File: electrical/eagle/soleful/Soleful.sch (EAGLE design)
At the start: 115 parts, among them IC1 STM32F405RGT, IC2 MCP1703DB, IC3 STM32F405RGT, Q1 MOSFET-PCHANNEL, Q2 8MHz, Q3 32.768kHz, Q4 32.768kHz, SW1 RST, SW2 USR, U1 MCP1802, Y1 12 MHz

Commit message: More work
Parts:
- added CN1: (no value), microbuilder:JST_2PIN
- added U3: MIC2090-1YM5TR, Micrel_By_element14_Batch_1:MIC2090-1YM5TR
- Q1: value MOSFET-PCHANNEL -> MOSFET
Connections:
- removed net N$10: Q1.D
- new net B: U3.EN
- new net VBAT: CN1.1, Q1.D
- new net VBUS: D1.ANODE, Q1.G, R10.2, R18.2, U$10.VUSB, U3.VOUT
- net 3V3: no longer D1.CATHODE, Q1.S
- net GND: now also CN1.2, U3.GND
- net N$8: now also U3.FAULT/; no longer D1.ANODE, Q1.G, R10.2, R18.2, U$10.VUSB
- net V+: now also D1.CATHODE, Q1.S, U3.VIN
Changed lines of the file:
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@@
 <part name="R18" library="SparkFun-Resistors" deviceset="100KOHM" device="-0603-1/10W-1%" value="100k"/>
 <part name="GND19" library="SparkFun-PowerSymbols" deviceset="GND" device=""/>
-<part name="Q1" library="User-Submitted" deviceset="MOSFET-PCHANNEL" device=""/>
-<part name="SUPPLY10" library="SparkFun-PowerSymbols" deviceset="VCC" device="" value="3V3"/>
+<part name="Q1" library="User-Submitted" deviceset="MOSFET-PCHANNEL" device="" value="MOSFET"/>
 <part name="GND20" library="supply1" deviceset="GND" device=""/>
 <part name="GND21" library="supply1" deviceset="GND" device=""/>
@@
 <part name="R37" library="rcl" deviceset="R-EU_" device="R0603" value="10k"/>
 <part name="R38" library="rcl" deviceset="R-EU_" device="R0805" value="0"/>
+<part name="U3" library="Micrel_By_element14_Batch_1" deviceset="MIC2090-1YM5TR" device=""/>
+<part name="GND42" library="Icotech_Eagle_Library" deviceset="GND" device=""/>
+<part name="SUPPLY11" library="SparkFun-PowerSymbols" deviceset="VCC" device="" value="V+"/>
+<part name="CN1" library="microbuilder" deviceset="JST_2PIN" device=""/>
+<part name="GND43" library="Icotech_Eagle_Library" deviceset="GND" device=""/>
+<part name="SUPPLY10" library="SparkFun-PowerSymbols" deviceset="VCC" device="" value="V+"/>
 </parts>
 <sheets>
@@
 <instance part="GND19" gate="1" x="238.76" y="233.68"/>
 <instance part="Q1" gate="G$1" x="228.6" y="259.08" rot="R90"/>
+<instance part="U3" gate="A" x="185.42" y="243.84"/>
+<instance part="GND42" gate="1" x="167.64" y="228.6"/>
+<instance part="SUPPLY11" gate="G$1" x="160.02" y="256.54"/>
+<instance part="CN1" gate="G$1" x="203.2" y="261.62"/>
+<instance part="GND43" gate="1" x="200.66" y="254"/>
 <instance part="SUPPLY10" gate="G$1" x="251.46" y="261.62"/>
 </instances>
@@
 <pinref part="C14" gate="G$1" pin="1"/>
 </segment>
-<segment>
-<pinref part="D1" gate="G$1" pin="CATHODE"/>
-<wire x1="243.84" y1="226.06" x2="251.46" y2="226.06" width="0.1524" layer="91"/>
-<wire x1="254" y1="226.06" x2="251.46" y2="226.06" width="0.1524" layer="91"/>
-<wire x1="251.46" y1="226.06" x2="251.46" y2="259.08" width="0.1524" layer="91"/>
-<pinref part="Q1" gate="G$1" pin="S"/>
-<wire x1="251.46" y1="259.08" x2="233.68" y2="259.08" width="0.1524" layer="91"/>
-<wire x1="251.46" y1="259.08" x2="251.46" y2="261.62" width="0.1524" layer="91"/>
-<junction x="251.46" y="259.08"/>
-<pinref part="SUPPLY10" gate="G$1" pin="VCC"/>
-</segment>
 </net>
 <net name="PB15-Y8" class="0">
@@
 <pinref part="GND19" gate="1" pin="GND"/>
 </segment>
+<segment>
+<pinref part="U3" gate="A" pin="GND"/>
+<wire x1="167.64" y1="236.22" x2="167.64" y2="231.14" width="0.1524" layer="91"/>
+<pinref part="GND42" gate="1" pin="GND"/>
+</segment>
+<segment>
+<pinref part="CN1" gate="G$1" pin="2"/>
+<wire x1="200.66" y1="261.62" x2="200.66" y2="256.54" width="0.1524" layer="91"/>
+<pinref part="GND43" gate="1" pin="GND"/>
+</segment>
 </net>
 <net name="N$1" class="0">
@@
 <pinref part="SUPPLY7" gate="G$1" pin="VCC"/>
 </segment>
+<segment>
+<pinref part="U3" gate="A" pin="VIN"/>
+<wire x1="167.64" y1="246.38" x2="160.02" y2="246.38" width="0.1524" layer="91"/>
+<wire x1="160.02" y1="246.38" x2="160.02" y2="256.54" width="0.1524" layer="91"/>
+<pinref part="SUPPLY11" gate="G$1" pin="VCC"/>
+</segment>
+<segment>
+<pinref part="D1" gate="G$1" pin="CATHODE"/>
+<wire x1="243.84" y1="226.06" x2="251.46" y2="226.06" width="0.1524" layer="91"/>
+<wire x1="251.46" y1="226.06" x2="251.46" y2="259.08" width="0.1524" layer="91"/>
+<pinref part="Q1" gate="G$1" pin="S"/>
+<wire x1="251.46" y1="259.08" x2="233.68" y2="259.08" width="0.1524" layer="91"/>
+<wire x1="251.46" y1="259.08" x2="251.46" y2="261.62" width="0.1524" layer="91"/>
+<junction x="251.46" y="259.08"/>
+<pinref part="SUPPLY10" gate="G$1" pin="VCC"/>
+</segment>
 </net>
 <net name="N$4" class="0">
@@
 </segment>
 </net>
-<net name="N$8" class="0">
+<net name="VBUS" class="0">
 <segment>
 <pinref part="U$10" gate="G$1" pin="VUSB"/>
@@
 <pinref part="Q1" gate="G$1" pin="G"/>
 <wire x1="228.6" y1="251.46" x2="233.68" y2="251.46" width="0.1524" layer="91"/>
-</segment>
-</net>
-<net name="N$10" class="0">
+<label x="226.06" y="226.06" size="1.778" layer="95"/>
+<wire x1="226.06" y1="226.06" x2="215.9" y2="226.06" width="0.1524" layer="91"/>
+<wire x1="215.9" y1="226.06" x2="215.9" y2="238.76" width="0.1524" layer="91"/>
+<junction x="226.06" y="226.06"/>
+<wire x1="215.9" y1="238.76" x2="203.2" y2="238.76" width="0.1524" layer="91"/>
+<pinref part="U3" gate="A" pin="VOUT"/>
+<wire x1="203.2" y1="243.84" x2="203.2" y2="238.76" width="0.1524" layer="91"/>
+</segment>
+</net>
+<net name="VBAT" class="0">
 <segment>
 <pinref part="Q1" gate="G$1" pin="D"/>
 <wire x1="223.52" y1="259.08" x2="210.82" y2="259.08" width="0.1524" layer="91"/>
-<wire x1="210.82" y1="259.08" x2="210.82" y2="261.62" width="0.1524" layer="91"/>
-</segment>
-</net>
+<pinref part="CN1" gate="G$1" pin="1"/>
+<wire x1="200.66" y1="264.16" x2="200.66" y2="269.24" width="0.1524" layer="91"/>
+<wire x1="200.66" y1="269.24" x2="210.82" y2="269.24" width="0.1524" layer="91"/>
+<wire x1="210.82" y1="269.24" x2="210.82" y2="259.08" width="0.1524" layer="91"/>
+<wire x1="210.82" y1="269.24" x2="210.82" y2="271.78" width="0.1524" layer="91"/>
+<junction x="210.82" y="269.24"/>
+<label x="208.28" y="271.78" size="1.778" layer="95"/>
+</segment>
+</net>
+<net name="N$8" class="0">
+<segment>
+<pinref part="U3" gate="A" pin="FAULT/"/>
+<wire x1="203.2" y1="246.38" x2="210.82" y2="246.38" width="0.1524" layer="91"/>
+</segment>
+</net>
+<net name="B" class="0">
+<segment>
+<pinref part="U3" gate="A" pin="EN"/>
+<wire x1="167.64" y1="241.3" x2="154.94" y2="241.3" width="0.1524" layer="91"/>
+<label x="162.56" y="241.3" size="1.778" layer="95"/>
+</segment>
+</net>

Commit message: Finally worked
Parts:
- removed C11B, C12B: 2u2, rcl:C-EUC0603
- removed C21, C22, C23, C24, C25, C26, C31, C32, C33: 100n, rcl:C-EUC0603
- removed C27, C28, C34, C35: 12p, rcl:C-EUC0603
- removed C29, C36, C37: 1u, rcl:C-EUC0603
- removed C30: 4u7, rcl:C-EUC0603
- removed D6: 1N5819, pyboard:1N5819
- removed IC3: STM32F405RGT, pyboard:STM32F405RGT
- removed JBL, JBR1, JBR2, JBR3, JBR4: 1, pinhead:PINHD-1X1
- removed JBOT: 8, pinhead:PINHD-1X8
- removed JLEFT: 14, pinhead:PINHD-1X14
- removed JPOW: 8, pinhead:PINHD-2X4
- removed JRIGHT: 11, pinhead:PINHD-1X11
- removed Q2: 8MHz, pyboard:TXC-CRYSTAL50X32
- removed Q3: 32.768kHz, pyboard:TXC-CRYSTAL32X15
- removed R19, R22: 22, rcl:R-EU_R0603
- removed R23, R37: 10k, rcl:R-EU_R0603
- removed R24, R25, R26, R27: 560, rcl:R-EU_R0603
- removed R28, R29: 4k7, rcl:R-EU_R0603
- removed R30, R31: 1k, rcl:R-EU_R0603
- removed R32, R34, R35: 100k, rcl:R-EU_R0603
- removed R33: 10M, rcl:R-EU_R0603
- removed R36: 0, rcl:R-EU_R0603
- removed R38: 0, rcl:R-EU_R0805
- removed U$2, U$3: KMR4TACTILE, pyboard:KMR4TACTILE
- removed U$4: MOLEX-SD-105027, pyboard:MOLEX-SD-105027
- removed U$5: MMA7660, pyboard:MMA7660
- removed U$6, U$7: LTST-C195KGJRKT, pyboard:LTST-C195KGJRKT
- removed U$8: USB-MICRO-AB, pyboard:USB-MICRO-AB
- removed U1: MCP1802, pyboard:MCP1802
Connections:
- removed net +3V3: C21.1, C22.1, C23.1, C24.1, C25.1, C26.1, C29.1, C30.1, C32.1, C37.1, IC3.VBAT, IC3.VDD@19, IC3.VDD@32, IC3.VDD@48, IC3.VDD@64, IC3.VDDA, JBL.1, JLEFT.1, R23.1, R28.1, R29.1, U$4.VDD, U$5.DVDD, U$6.A1, U$6.A2, U$7.A1, U$7.A2, U1.VOUT
- removed net BOOT0: IC3.BOOT0, JBOT.1, R35.1
- removed net FS_DM: IC3.PA11, R19.2
- removed net FS_DP: IC3.PA12, R22.2
- removed net FS_VUSB: IC3.PA9, R30.2
- removed net IO_PA0: IC3.PA0, JBR4.1
- removed net IO_PA1: IC3.PA1, JBR3.1
- removed net IO_PA14: IC3.PA14, JLEFT.9
- removed net IO_PA15: IC3.PA15, JLEFT.10
- removed net IO_PA2: IC3.PA2, JBR2.1
- removed net IO_PA3: IC3.PA3, JBR1.1
- removed net IO_PA4: IC3.PA4, JRIGHT.11
- removed net IO_PA5: IC3.PA5, JRIGHT.10
- removed net IO_PA6: IC3.PA6, JRIGHT.9
- removed net IO_PA7: IC3.PA7, JRIGHT.8
- removed net IO_PB0: IC3.PB0, JRIGHT.7
- removed net IO_PB1: IC3.PB1, JRIGHT.6
- removed net IO_PB10: IC3.PB10, JRIGHT.5
- removed net IO_PB11: IC3.PB11, JRIGHT.4, R32.1
- removed net IO_PB12: IC3.PB12, JRIGHT.3
- removed net IO_PB13: IC3.PB13, JLEFT.3
- removed net IO_PB14: IC3.PB14, JLEFT.4
- removed net IO_PB15: IC3.PB15, JLEFT.5
- removed net IO_PB2: IC3.PB2, R31.1
- removed net IO_PB3: IC3.PB3, JLEFT.11
- removed net IO_PB4: IC3.PB4, JLEFT.12
- removed net IO_PB9: IC3.PB9, JBOT.4
- removed net IO_PC0: IC3.PC0, JBOT.5
- removed net IO_PC1: IC3.PC1, JBOT.6
- removed net IO_PC2: IC3.PC2, JBOT.7
- removed net IO_PC3: IC3.PC3, JBOT.8
- removed net IO_PC6: IC3.PC6, JLEFT.6
- removed net IO_PC7: IC3.PC7, JLEFT.7
- removed net LEDG1: IC3.PC4, R24.1
- removed net LEDG2: IC3.PC5, R27.1
- removed net LEDR1: IC3.PA8, R26.1
- removed net LEDR2: IC3.PA10, R25.1, R36.2
- removed net MMA_AVDD: C33.1, IC3.PB5, R34.1, U$5.AVDD
- removed net MMA_INT: IC3.PB8, JBOT.3, U$5.INT
- removed net MMA_SCL: IC3.PB6, JLEFT.13, R29.2, U$5.SCL
- removed net MMA_SDA: IC3.PB7, JLEFT.14, R28.2, U$5.SDA
- removed net N$11: C12B.1, IC3.VCAP_1
- removed net N$12: R22.1, U$8.D+
- removed net N$13: C28.2, IC3.PH0, Q2.P$1
- removed net N$14: R24.2, U$6.K1
- removed net N$15: R25.2, U$7.K2
- removed net N$16: R26.2, U$6.K2
- removed net N$17: C35.2, IC3.PC14, Q3.P$1
- removed net N$18: C34.2, IC3.PC15, Q3.P$2
- removed net N$19: C27.2, IC3.PH1, Q2.P$2
- removed net N$20: R27.2, U$7.K1
- removed net N$21: R19.1, U$8.D-
- removed net N$22: R36.1, U$8.ID
- removed net N$23: R37.2, U$3.1@A, U$3.1@B
- removed net N$9: C11B.1, IC3.VCAP_2
- removed net NRST: C31.1, IC3.NRST, JBOT.2, R23.2, U$2.1@A, U$2.1@B
- removed net SDIO_CK: IC3.PC12, U$4.CLK
- removed net SDIO_CMD: IC3.PD2, U$4.CMD
- removed net SDIO_D0: IC3.PC8, U$4.DAT0
- removed net SDIO_D1: IC3.PC9, U$4.DAT1
- removed net SDIO_D2: IC3.PC10, U$4.DAT2
- removed net SDIO_D3: IC3.PC11, R33.1, U$4.DAT3
- removed net SDIO_SW: IC3.PC13, U$4.SWITCH
- removed net USR_SW: IC3.PA13, JLEFT.8, R37.1
- removed net VIN: C36.1, D6.K, JPOW.2, JPOW.4, JPOW.6, JPOW.8, JRIGHT.1, R38.1, U1.EN, U1.VIN
- removed net VUSB: D6.A, R30.1, R38.2, U$8.VUSB
- net GND: no longer C11B.2, C12B.2, C21.2, C22.2, C23.2, C24.2, C25.2, C26.2, C27.1, C28.1, C29.2, C30.2, C31.2, C32.2, C33.2, C34.1, C35.1, C36.2, C37.2, IC3.VSS@18, IC3.VSS@63, IC3.VSSA, JLEFT.2, JPOW.1, JPOW.3, JPOW.5, JPOW.7, JRIGHT.2, R31.2, R32.2, R33.2, R34.2, R35.2, U$2.0@A, U$2.0@B, U$3.0@A, U$3.0@B, U$4.VSS, U$5.AVSS, U$5.DVSS, U$5.N/C@10, U$5.N/C@2, U$5.RSRVD, U$8.GND, U1.GND
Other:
- note removed: "Analog"
- note removed: "DFU boot"
- note removed: "MMA"
- note removed: "R16 and R18 are unpopulated. Used for optional USB OTG support."
- note removed: "VBAT"
- note removed: "VDD"

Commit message: Added IMU files
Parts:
- added C21, C22: 22pF, microbuilder:CAP_CERAMIC0805-NOOUTLINE
- added C23: 0.1uF, microbuilder:CAP_CERAMIC0805-NOOUTLINE
- added C24: 0.1uF, microbuilder:CAP_CERAMIC0805_10MGAP
- added D6: 1n4148, microbuilder:DIODESOD-323
- added Q2, Q3: BSS138, microbuilder:MOSFET-NWIDE
- added R19, R22, R23, R24, R25, R28: 10K, microbuilder:RESISTOR0805_NOOUTLINE
- added R26, R27: 10K, microbuilder:RESISTOR_0805MP
- added U$2: (no value), esp8266modules:OLIMEX_MOD-WIFI-ESP8266-DEV>PINS-INSIDE
- added U$4: BNO055, microbuilder:BNO055
- added Y2: 32.768kHz, microbuilder:CRYSTAL8.0X3.8
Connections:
- new net 5.0V: R26.2, R27.2
- new net I2CADDR_3V: R23.1, U$4.COM3/I2C_ADDR
- new net INT_3V: U$4.INT
- new net N$55: C21.2, U$4.XIN32, Y2.2
- new net N$56: C22.2, U$4.XOUT32, Y2.1
- new net N$57: C23.2, U$4.CAP
- new net NRESET_3V: D6.A, R28.1, U$4.NRESET
- new net PS0_3V: R19.1, U$4.PS0
- new net PS1_3V: R22.1, U$4.PS1
- new net RST_5V: D6.C
- new net SCL_3V: Q3.S, R25.1, U$4.COM1/SCL/RX
- new net SCL_5V: Q3.D, R27.1
- new net SDA_3V: Q2.S, R24.1, U$4.COM0/SDA/TX
- new net SDA_5V: Q2.D, R26.1
- net 3V3: now also C24.2, Q2.G, Q3.G, R24.2, R25.2, R28.2, U$4.NBOOT_LOAD_PIN, U$4.VDD, U$4.VDDIO
- net GND: now also C21.1, C22.1, C23.1, C24.1, R19.2, R22.2, R23.2, U$4.COM2(GND), U$4.GND@1, U$4.GND@2, U$4.PIN10(GND), U$4.PIN15(GND), U$4.PIN16(GND)

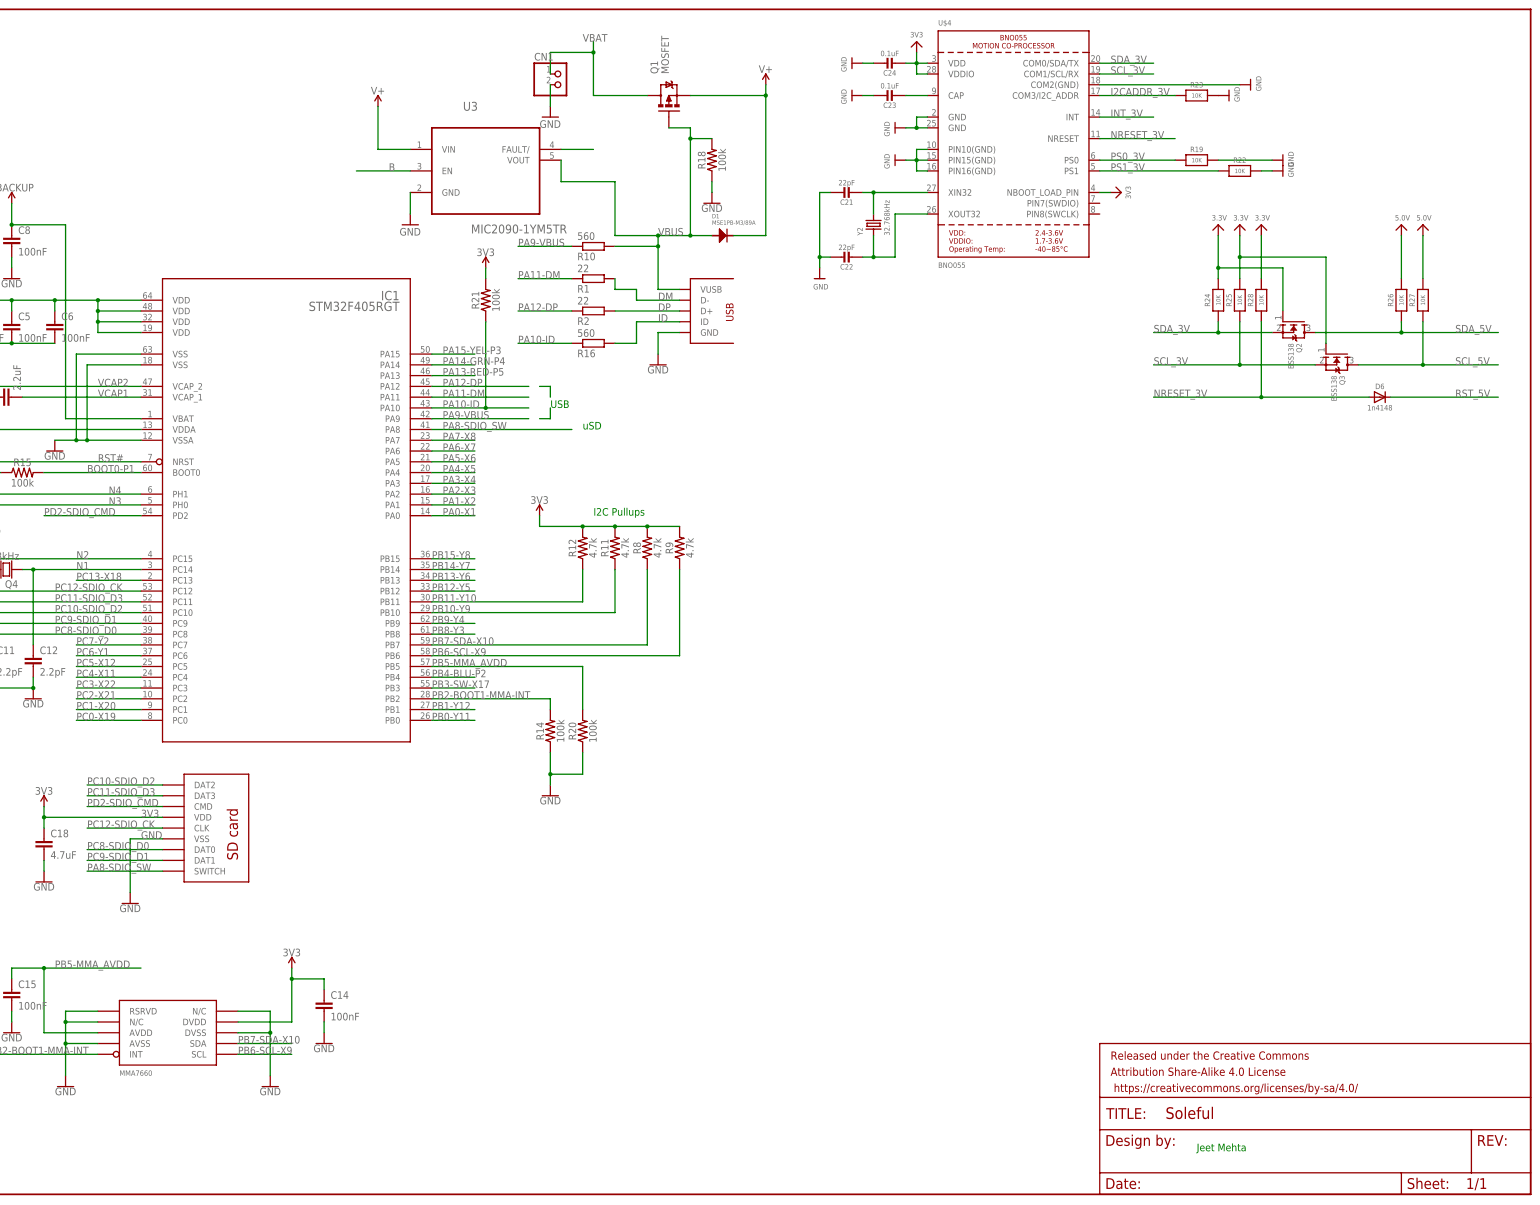
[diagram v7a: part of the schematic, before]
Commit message: Finished IMU, added FSRs
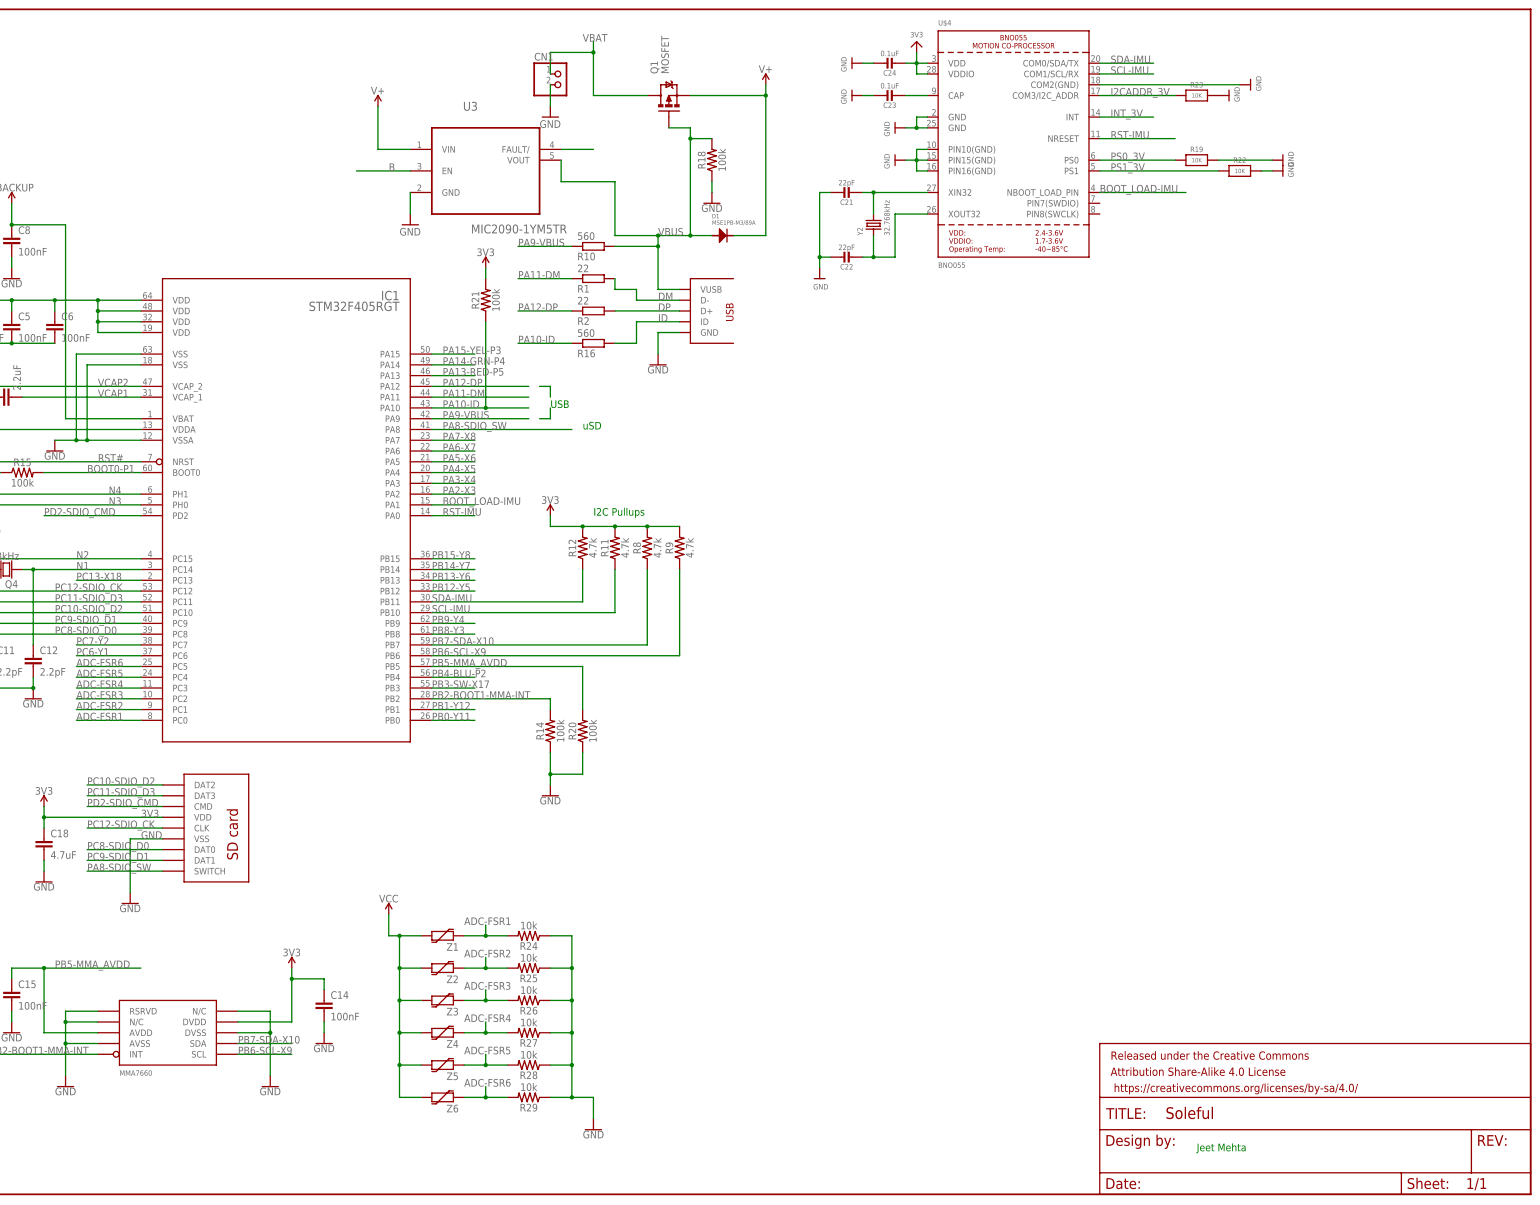
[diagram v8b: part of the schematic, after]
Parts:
- removed D6: 1n4148, microbuilder:DIODESOD-323
- removed Q2, Q3: BSS138, microbuilder:MOSFET-NWIDE
- added R29: 10k, SparkFun-Resistors:10KOHM-0603-1/10W-1%
- added Z1, Z2, Z3, Z4, Z5, Z6: (no value), SparkFun-DiscreteSemi:VARISTOR-0402
- R24, R25, R28: value 10K -> 10k; device microbuilder:RESISTOR0805_NOOUTLINE -> SparkFun-Resistors:10KOHM-0603-1/10W-1%
- R26, R27: value 10K -> 10k; device microbuilder:RESISTOR_0805MP -> SparkFun-Resistors:10KOHM-0603-1/10W-1%
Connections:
- removed net 5.0V: R26.2, R27.2
- removed net NRESET_3V: D6.A, R28.1, U$4.NRESET
- removed net PA0-X1: IC1.PA0
- removed net PA1-X2: IC1.PA1
- removed net PB10-Y9: IC1.PB10, R11.1
- removed net PB11-Y10: IC1.PB11, R12.1
- removed net PC0-X19: IC1.PC0
- removed net PC1-X20: IC1.PC1
- removed net PC2-X21: IC1.PC2
- removed net PC3-X22: IC1.PC3
- removed net PC4-X11: IC1.PC4
- removed net PC5-X12: IC1.PC5
- removed net RST_5V: D6.C
- removed net SCL_3V: Q3.S, R25.1, U$4.COM1/SCL/RX
- removed net SCL_5V: Q3.D, R27.1
- removed net SDA_3V: Q2.S, R24.1, U$4.COM0/SDA/TX
- removed net SDA_5V: Q2.D, R26.1
- new net ADC-FSR1: IC1.PC0, R24.2, Z1.1
- new net ADC-FSR2: IC1.PC1, R25.2, Z2.1
- new net ADC-FSR3: IC1.PC2, R26.2, Z3.1
- new net ADC-FSR4: IC1.PC3, R27.2, Z4.1
- new net ADC-FSR5: IC1.PC4, R28.2, Z5.1
- new net ADC-FSR6: IC1.PC5, R29.2, Z6.1
- new net BOOT_LOAD-IMU: IC1.PA1, U$4.NBOOT_LOAD_PIN
- new net RST-IMU: IC1.PA0, U$4.NRESET
- new net SCL-IMU: IC1.PB10, R11.1, U$4.COM1/SCL/RX
- new net SDA-IMU: IC1.PB11, R12.1, U$4.COM0/SDA/TX
- new net VCC: Z1.2, Z2.2, Z3.2, Z4.2, Z5.2, Z6.2
- net 3V3: no longer Q2.G, Q3.G, R24.2, R25.2, R28.2, U$4.NBOOT_LOAD_PIN
- net GND: now also R24.1, R25.1, R26.1, R27.1, R28.1, R29.1
